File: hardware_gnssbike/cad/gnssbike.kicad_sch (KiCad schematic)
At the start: 0 parts

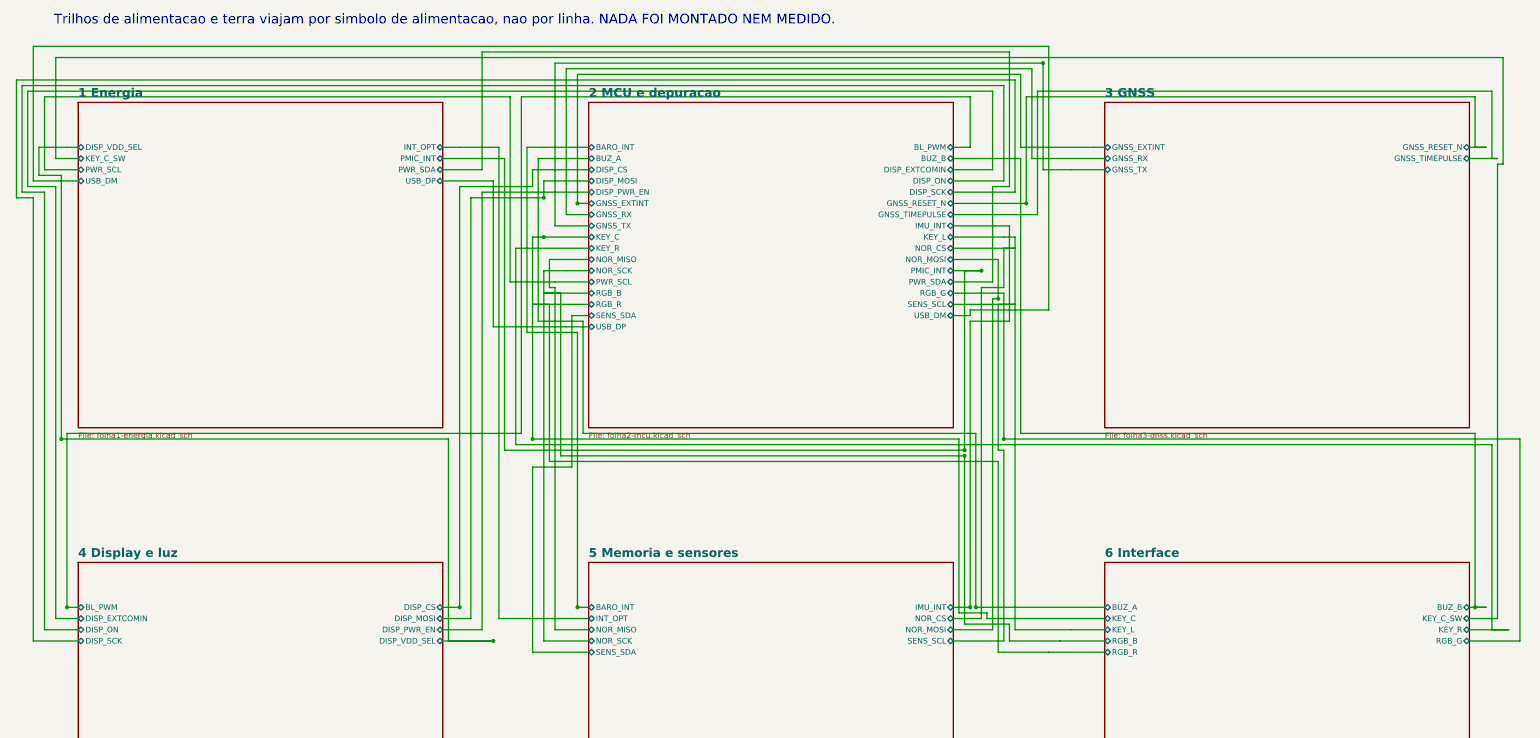
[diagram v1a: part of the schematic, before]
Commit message: feat(hardware): GNSS receiver on the 3V0 rail, and the electrical items closed with the owner
The receiver ran at 1.8 V from BUCK1 through a TXU0204 level shifter, and
table 35 of the MAX-F10S integration manual asks +-2 % of a 1.8 V supply
where the nPM1300 buck gives +-5 %. A +-1 % LDO from 3V0 fixed the
tolerance and cost 35 mW at the battery (the receiver paid at 3.0 V with
1.2 V burnt in the LDO); option 1 of the same table - VCC and V_IO tied at
3.0 V, VIO_SEL open - costs 11 mW and removes the shifter. The owner chose
option 1. The receiver now sits on 3V0 through JP103 and the ferrite, the
four digital lines go pin to pin, the shifter and the LDO leave with four
capacitors, and BUCK1 stays fitted and unloaded as in configuration 1 of
the nPM1300 datasheet (the datasheet only shows an unused BUCK2, and what
it does not show is not copied). The devicetree follows: vcc-supply on
BUCK2, BUCK1 regulator-boot-off. The receiver no longer has a rail that
switches off; that consequence is recorded in docs/10.

Closed the same day, each a decision of the owner or a datasheet fact:

  - the ADP5091 TERM and SETSD dividers hung from BAT with REF open;
    figure 42 of the datasheet hangs all four external dividers from REF,
    which the chip switches to BAT with the hysteresis resistor in series.
    Equation 6 did not hold as drawn. Net ADP_REF, same values.
  - the solar charge thermal cut-off: the ADP5091 has no temperature
    input and the NTC divider was on the board with nobody reading it. A
    TLV7031 fed from the panel compares RT101/R106 with half of SRC and
    pulls DIS_SW high through a BAT54WS, in diode-OR with the USB divider.
    Hot side only; charging below 0 C stays open, and says so.
  - the centre key reaches P1.27 through a Schottky (D107): the SHPHLD
    node rises to 5.5 V with the cable.
  - J102 copper matched to the pinout 06 sends to the pack maker: the
    copper had VBAT+ on 1, NTC on 4, GND on 6 and 2, 3 and 5 open.
  - FB301 with 150 mO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
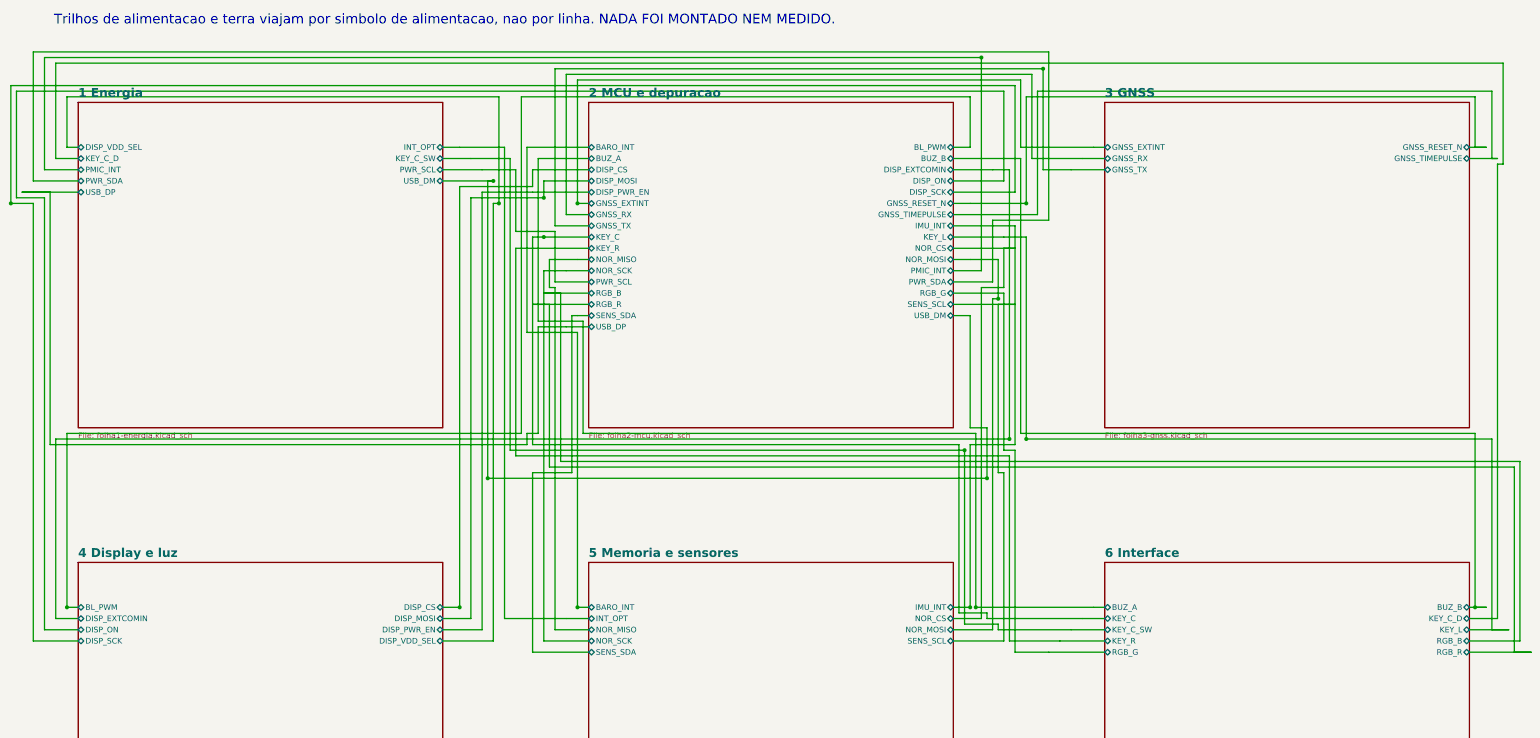
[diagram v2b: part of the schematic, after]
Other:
- sheet 1 Energia ports: added KEY_C_D; removed none
- sheet 6 Interface ports: added KEY_C_D; removed none

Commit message: feat(hardware): draw the schematic by functional block, the way a person reads it
The owner asked for an industrial-standard schematic: wires and labels,
A4 or A3 pages, the right symbols and values, easy to read, the circuits
subdivided by dashed boxes. Until now each sheet was the netlist drawn as
wires - parts on a grid in connection order and a maze router pulling a
wire from every pin to wherever its other end was, across the page.

blocos.py turns each sheet into a row of functional blocks in the order
the signal flows, each in a dashed rectangle with a title: on the power
sheet, USB-C and protection, the nPM1300, the gauge and the cell, the GNSS
backup, the solar harvester, the thermal cut-off. Membership comes from
the BLOCOS table (the anchors), then make_pcb.DECOPLA and JUNTO (the
board already says whose each capacitor is), then sheets.SEGUE, then the
netlist without rails, nearest anchor by hops. Inside a block the anchor
sits in the middle and each passive beside the pin it serves, on the
side that pin faces, mirrored when the pin that serves the chip is the
far one; parts that touch only rails go to a shelf under the chip. Rails
are power symbols, neighbouring pins of one rail get a wire along their
tips and one symbol; a net that leaves its block is a local label, one
that leaves the sheet a hierarchical label, both on a short stub the
maze router bends when the straight way is taken. Sheet 1 is A3, the
rest A4, measured by the drawing itself. Decoupling capacitors now live
on their chip's sheet whatever their number.

Three KiCad 8 facts were measured with kicad-cli's netlist export on the
way, because the first version assumed each one wrong and check_sch.py
caught it: (mirror x) swaps left for right, not (mirror y); a local label
named after a rail is the net /sheet/RAIL, another net; and a pin in the
middle of a long wire is not on it - "wires connect with other wires or
pins only if their ends coincide exactly" (Eeschema manual). The
conventions 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
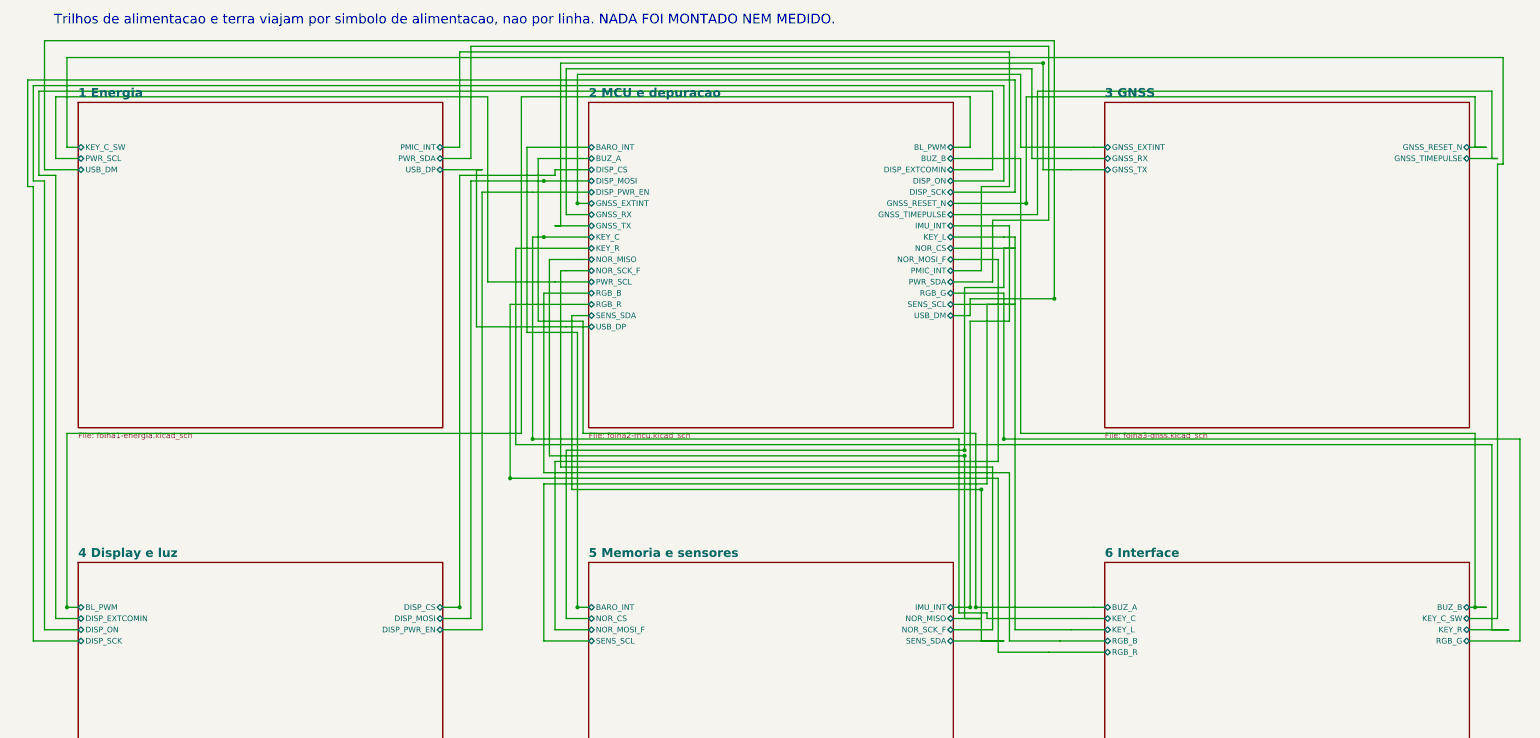
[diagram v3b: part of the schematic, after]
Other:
- sheet 1 Energia ports: added none; removed DISP_VDD_SEL, INT_OPT, KEY_C_D
- sheet 2 MCU e depuracao ports: added NOR_MOSI_F, NOR_SCK_F; removed NOR_MOSI, NOR_SCK
- sheet 4 Display e luz ports: added none; removed DISP_VDD_SEL
- sheet 5 Memoria e sensores ports: added NOR_MOSI_F, NOR_SCK_F; removed INT_OPT, NOR_MOSI, NOR_SCK
- sheet 6 Interface ports: added none; removed KEY_C_D
